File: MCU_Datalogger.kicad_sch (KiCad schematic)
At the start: 25 parts, among them U1 24LC1025, U2 24LC1025, U3 ATMEGA328P-AU, U4 DS1337S_, Y1 Crystal, Y2 Crystal

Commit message: Values Added
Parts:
- C1, C4: value C -> 0.1uF
- C2: renamed from C3; value C -> 22pF
- C3: renamed from C2; value C -> 22pF
- C5: value C_Polarized -> 100 nF
- R1: renamed from R5; value R -> 10K
- R2: renamed from R4; value R -> 10K
- R3: renamed from R2; value R -> 4.7K
- R4: renamed from R3; value R -> 4.7K
- R5: renamed from R6; value R -> 330
- R6: renamed from R1; value R -> 10K
- R7: value R -> 330
- Y1: renamed from Y2; value Crystal -> 32.768 KHz
- Y2: renamed from Y1; value Crystal -> 16 MHz
- renumbered U4 to U1, U1 to U2, U2 to U3, U3 to U4
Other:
- moved on the sheet: BT1, C1, C2, C3, C4, C5, D1, D2, H1, H2, H3, H4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

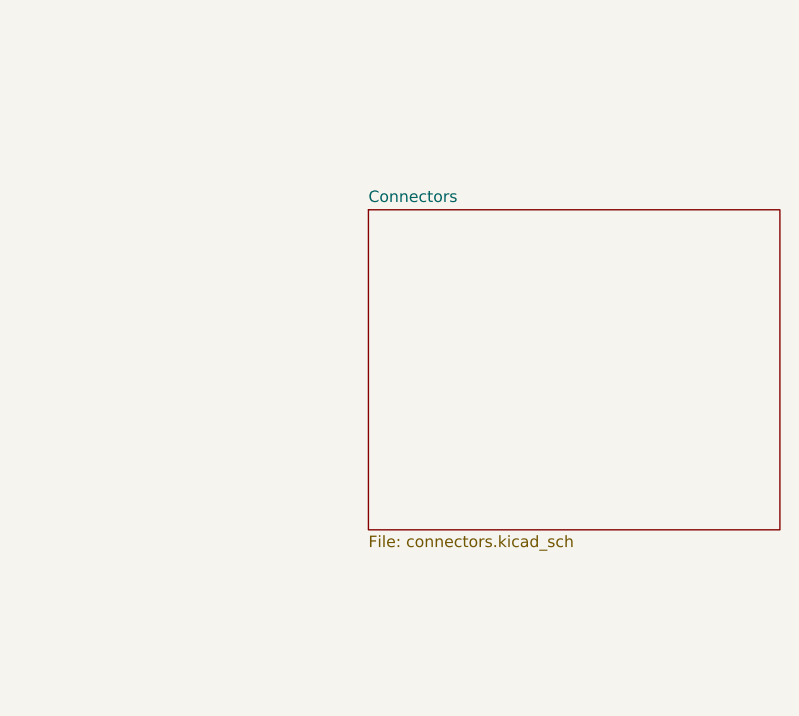
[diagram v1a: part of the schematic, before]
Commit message: Problems in connectors fixed
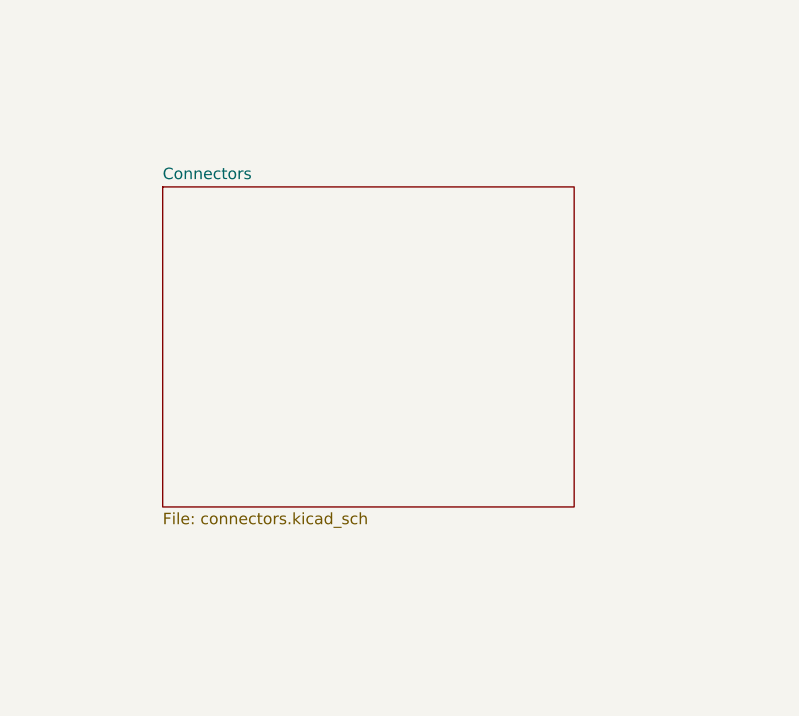
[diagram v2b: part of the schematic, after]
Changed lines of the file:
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@@
 	)
 	(sheet
-		(at 226.06 113.03)
+		(at 203.2 110.49)
 		(size 45.72 35.56)
 		(exclude_from_sim no)
@@
 		)
 		(property "Sheetname" "Connectors"
-			(at 226.06 112.3184 0)
+			(at 203.2 109.7784 0)
 			(show_name yes)
 			(effects
@@
 		)
 		(property "Sheetfile" "connectors.kicad_sch"
-			(at 226.06 149.1746 0)
+			(at 203.2 146.6346 0)
 			(show_name yes)
 			(effects

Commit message: Symbol to Footprint Association
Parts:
- BT1: footprint (none) -> Connector_PinHeader_2.54mm:PinHeader_1x02_P2.54mm_Vertical
- C1, C2, C3, C4, C5: footprint (none) -> Capacitor_SMD:C_0805_2012Metric
- D1, D2: footprint (none) -> LED_SMD:LED_0805_2012Metric
- H1, H2, H3, H4: footprint (none) -> MountingHole:MountingHole_2.1mm
- R1, R2, R3, R4, R5, R6, R7: footprint (none) -> Resistor_SMD:R_0805_2012Metric
- U1: footprint DS1337S_:SOIC127P600X175-8N -> Footprint:SOIC127P600X175-8N
- U2, U3: footprint (none) -> Package_SO:SOIC-8_5.3x5.3mm_P1.27mm
- U4: footprint ATMEGA328P-AU:QFP80P900X900X120-32N -> Footprint:QFP80P900X900X120-32N
- Y1, Y2: footprint (none) -> Crystal:Crystal_SMD_5032-2Pin_5.0x3.2mm_HandSoldering
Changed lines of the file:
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@@
 			)
 		)
-		(property "Footprint" ""
+		(property "Footprint" "MountingHole:MountingHole_2.1mm"
 			(at 158.75 171.45 0)
 			(effects
@@
 			)
 		)
-		(property "Footprint" ""
+		(property "Footprint" "Resistor_SMD:R_0805_2012Metric"
 			(at 102.362 128.27 90)
 			(effects
@@
 			)
 		)
-		(property "Footprint" ""
+		(property "Footprint" "LED_SMD:LED_0805_2012Metric"
 			(at 238.76 46.99 0)
 			(effects
@@
 			)
 		)
-		(property "Footprint" ""
+		(property "Footprint" "Package_SO:SOIC-8_5.3x5.3mm_P1.27mm"
 			(at 83.82 129.54 0)
 			(effects
@@
 			)
 		)
-		(property "Footprint" ""
+		(property "Footprint" "Package_SO:SOIC-8_5.3x5.3mm_P1.27mm"
 			(at 54.61 129.54 0)
 			(effects
@@
 			)
 		)
-		(property "Footprint" ""
+		(property "Footprint" "Crystal:Crystal_SMD_5032-2Pin_5.0x3.2mm_HandSoldering"
 			(at 25.4 62.23 0)
 			(effects
@@
 			)
 		)
-		(property "Footprint" ""
+		(property "Footprint" "Capacitor_SMD:C_0805_2012Metric"
 			(at 151.4348 66.04 0)
 			(effects
@@
 			)
 		)
-		(property "Footprint" ""
+		(property "Footprint" "Resistor_SMD:R_0805_2012Metric"
 			(at 90.932 53.34 90)
 			(effects
@@
 			)
 		)
-		(property "Footprint" ""
+		(property "Footprint" "Resistor_SMD:R_0805_2012Metric"
 			(at 180.34 83.058 90)
 			(effects
@@
 			)
 		)
-		(property "Footprint" ""
+		(property "Footprint" "Capacitor_SMD:C_0805_2012Metric"
 			(at 186.69 30.7848 0)
 			(effects
@@
 			)
 		)
-		(property "Footprint" ""
+		(property "Footprint" "Capacitor_SMD:C_0805_2012Metric"
 			(at 106.3752 57.15 0)
 			(effects
@@
 			)
 		)
-		(property "Footprint" ""
+		(property "Footprint" "Connector_PinHeader_2.54mm:PinHeader_1x02_P2.54mm_Vertical"
 			(at 259.08 35.306 90)
 			(effects
@@
 			)
 		)
-		(property "Footprint" ""
+		(property "Footprint" "Capacitor_SMD:C_0805_2012Metric"
 			(at 153.3652 59.69 0)
 			(effects
@@
 			)
 		)
-		(property "Footprint" "ATMEGA328P-AU:QFP80P900X900X120-32N"
+		(property "Footprint" "Footprint:QFP80P900X900X120-32N"
 			(at 213.36 60.96 0)
 			(effects
@@
 			)
 		)
-		(property "Footprint" "DS1337S_:SOIC127P600X175-8N"
+		(property "Footprint" "Footprint:SOIC127P600X175-8N"
 			(at 58.42 66.04 0)
 			(effects
@@
 			)
 		)
-		(property "Footprint" ""
+		(property "Footprint" "MountingHole:MountingHole_2.1mm"
 			(at 158.75 161.29 0)
 			(effects
@@
 			)
 		)
-		(property "Footprint" ""
+		(property "Footprint" "Resistor_SMD:R_0805_2012Metric"
 			(at 238.252 59.69 90)
 			(effects
@@
 			)
 		)
-		(property "Footprint" ""
+		(property "Footprint" "Resistor_SMD:R_0805_2012Metric"
 			(at 152.4 47.498 90)
 			(effects
@@
 			)
 		)
-		(property "Footprint" ""
+		(property "Footprint" "MountingHole:MountingHole_2.1mm"
 			(at 158.75 189.23 0)
 			(effects
@@
 			)
 		)
-		(property "Footprint" ""
+		(property "Footprint" "Crystal:Crystal_SMD_5032-2Pin_5.0x3.2mm_HandSoldering"
 			(at 182.88 62.23 0)
 			(effects
@@
 			)
 		)
-		(property "Footprint" ""
+		(property "Footprint" "Resistor_SMD:R_0805_2012Metric"
 			(at 115.062 128.27 90)
 			(effects
@@
 			)
 		)
-		(property "Footprint" ""
+		(property "Footprint" "MountingHole:MountingHole_2.1mm"
 			(at 158.75 180.34 0)
 			(effects
@@
 			)
 		)
-		(property "Footprint" ""
+		(property "Footprint" "Resistor_SMD:R_0805_2012Metric"
 			(at 79.502 53.34 90)
 			(effects
@@
 			)
 		)
-		(property "Footprint" ""
+		(property "Footprint" "Capacitor_SMD:C_0805_2012Metric"
 			(at 239.7252 40.64 0)
 			(effects
@@
 			)
 		)
-		(property "Footprint" ""
+		(property "Footprint" "LED_SMD:LED_0805_2012Metric"
 			(at 182.88 45.72 0)
 			(effects

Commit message: Wiring done
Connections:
- net GND: now reaches R3.1
- net GND: now also BT1.2 (-), C1.1, C1.2, C2.1, C3.2, C4.2, C5.2, R1.1, R2.1, R4.1, R5.1, R6.1, R7.2, U1.4 (GND), U1.8 (VCC), U2.1 (A0), U2.2 (A1), U2.3 (A2), U2.4 (GND), U2.7 (WP), U2.8 (VCC), U3.1 (A0), U3.2 (A1), U3.3 (A2), U3.4 (GND), U3.7 (WP), U3.8 (VCC), U4.21 (GND), U4.3 (GND), U4.5 (GND)
- net SCK: now reaches R3.2
- net SCK: now also D1.2 (A), U1.6 (SCL), U2.6 (SCL), U3.6 (SCL), U4.17 (PB5), U4.28 (PC5)
- net at D2.1 (K): now also R7.1
- net at D2.2 (A): now also BT1.1 (+), C5.1, U4.18 (AVCC), U4.4 (VCC)
- net SDA: now reaches U3.5 (SDA)
- net SDA: now also R4.2, U1.5 (SDA), U2.5 (SDA), U4.27 (PC4)
- net at Y1.1: now also U1.2 (X2)
- net at Y1.2: now also U1.1 (X1)
- net at C3.1: now also U4.8 (PB7), Y2.1
- net at R2.2: now also U1.7 (SQW/~INT)
- net RESET: now reaches R6.2
- net RESET: now also U4.29 (PC6/~{RESET})
- net at C4.1: now also U4.20 (AREF)
- net at C2.2: now also U4.7 (PB6), Y2.2
- net D3: now reaches U4.1 (PD3)
- net D6: now reaches U4.10 (PD6)
- net D7: now reaches U4.11 (PD7)
- net D8: now reaches U4.12 (PB0)
- net MOSI: now reaches U4.15 (PB3)
- net MISO: now reaches U4.16 (PB4)
- net D4: now reaches U4.2 (PD4)
- net RX: now reaches U4.30 (PD0)
- net TX: now reaches U4.31 (PD1)
- net D2: now reaches U4.32 (PD2)
- net at U4.6 (VCC): no longer U4.4 (VCC)
- net D5: now reaches U4.9 (PD5)
- net at U1.3 (~{INTA}): now also R1.2
- net at R5.2: now also D1.1 (K)
- no-connect marks 0 -> 9
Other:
- sheet Connectors ports: added D2, D3, D4, D5, D6, D7, D8, GND, MISO, MOSI, RESET, RX, SCK, SDA, TX, Vcc; removed none
- moved on the sheet: BT1, C1, C2, C3, C4, C5, D1, D2, R1, R2, R5, R6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

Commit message: completed comments
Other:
- note added: "Connectors"
- note added: "EEPROM"
- note added: "MCU"
- note added: "Real Time Clock"
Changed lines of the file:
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@@
 		(date "2025-08-01")
+	)
+	(rectangle
+		(start 179.07 105.41)
+		(end 242.57 153.67)
+		(stroke
+			(width 0)
+			(type default)
+		)
+		(fill
+			(type none)
+		)
+	)
+	(rectangle
+		(start 29.21 21.59)
+		(end 133.35 95.25)
+		(stroke
+			(width 0)
+			(type default)
+		)
+		(fill
+			(type none)
+		)
+	)
+	(rectangle
+		(start 29.21 107.95)
+		(end 133.35 153.67)
+		(stroke
+			(width 0)
+			(type default)
+		)
+		(fill
+			(type none)
+		)
+	)
+	(rectangle
+		(start 143.51 17.78)
+		(end 283.21 99.06)
+		(stroke
+			(width 0)
+			(type default)
+		)
+		(fill
+			(type none)
+		)
+	)
+	(text "Real Time Clock"
+		(exclude_from_sim no)
+		(at 36.83 19.05 0)
+		(effects
+			(font
+				(size 1.27 1.27)
+			)
+		)
+	)
+	(text "Connectors"
+		(exclude_from_sim no)
+		(at 185.42 104.14 0)
+		(effects
+			(font
+				(size 1.27 1.27)
+			)
+		)
+	)
+	(text "EEPROM"
+		(exclude_from_sim no)
+		(at 33.02 106.68 0)
+		(effects
+			(font
+				(size 1.27 1.27)
+			)
+		)
+	)
+	(text "MCU\n"
+		(exclude_from_sim no)
+		(at 146.05 15.24 0)
+		(effects
+			(font
+				(size 1.27 1.27)
+			)
+		)
 	)
 	(junction
